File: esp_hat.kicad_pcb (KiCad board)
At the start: 2 copper layers, 65 x 30 mm, 40 parts, among them IC1 AT24CS32-STUM, J1 U.FL, P1 CONN_02X20, P2 CONN_01X03, P3 CONN_01X06, U1 ESP8266EX, U2 AP1117D33, Y1 26MHz

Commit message: Mostly done
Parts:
- added REF**: Symbol_OSHW-Logo_SilkScreen, Symbols:Symbol_OSHW-Logo_SilkScreen, F.Cu at (88.0, 94.3)
- R11: footprint mcuos:0603(1608m)-CHIP-RESISTOR -> mcuos:0603(1608m)
- U2: footprint esp_hat:SOT-223-gndslug -> TO_SOT_Packages_SMD:SOT-223
- W1, W2, W3, W4: footprint Mounting_Holes:MountingHole_3-5mm -> esp_hat:NPTH_Hole_3-5mm
- Y1: footprint mcuos:TXC-7V_xtal -> Crystals:crystal_FA238-TSX3225
- moved C1 0.14 mm to (106.2, 95.6)
- moved C3 0.06 mm to (100.3, 95.6)
- turned Y1 to 180 degrees
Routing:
- net GND: track 282.7 -> 536.7 mm, vias 19 -> 74
- net GPIO5: track 28.7 -> 32.7 mm
- net SD_D1: track 29.4 -> 30.9 mm
- net SD_CMD: track 33.2 -> 34.8 mm
- net SD_D0: track 28.6 -> 30.1 mm
- net SD_D3: track 32.4 -> 33.9 mm
- net SD_CLK: track 27.5 -> 29.0 mm
- net SD_D2: track 30.7 -> 31.8 mm
- net Net-(P2-Pad2): track 28.6 -> 29.3 mm
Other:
- net class 50ohm_oshpark: via_dia 0.6 -> 0.6858
- net class Default: via_dia 0.6 -> 0.6858
- rule trace_min: 0.2 -> 0.1524
- rule via_min_drill: 0.3 -> 0.3302
- rule via_min_size: 0.4 -> 0.6858
- board text added: "ESP HAT"

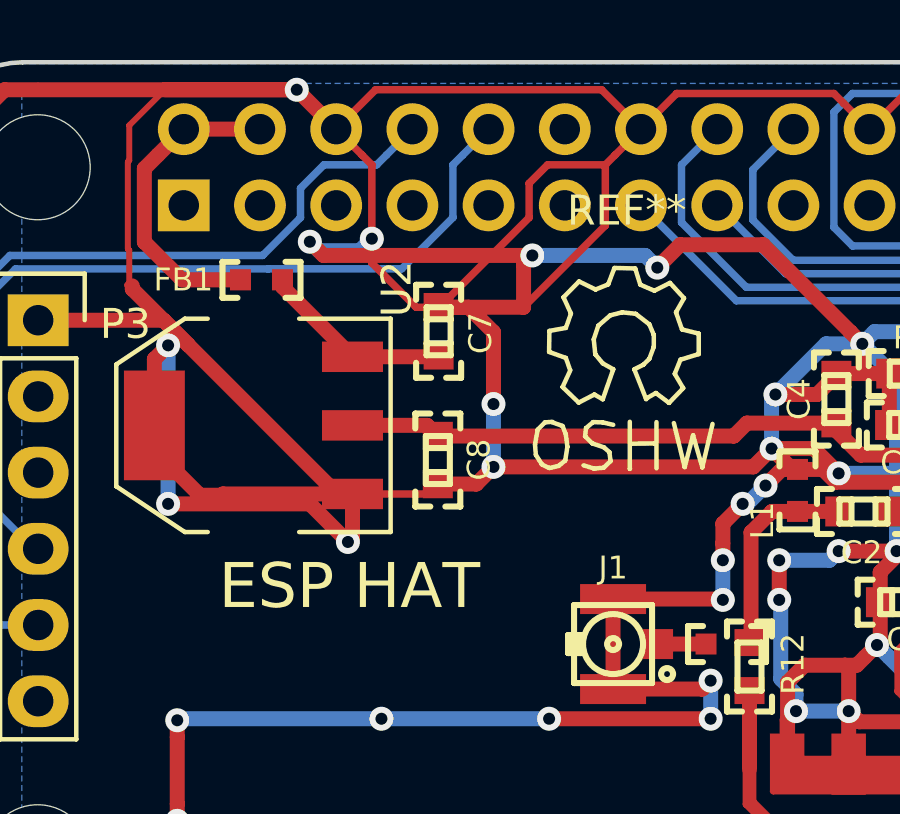
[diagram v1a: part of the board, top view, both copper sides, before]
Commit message: v0.1 to fab, moved text to back silk, changed license to CC-BY-SA
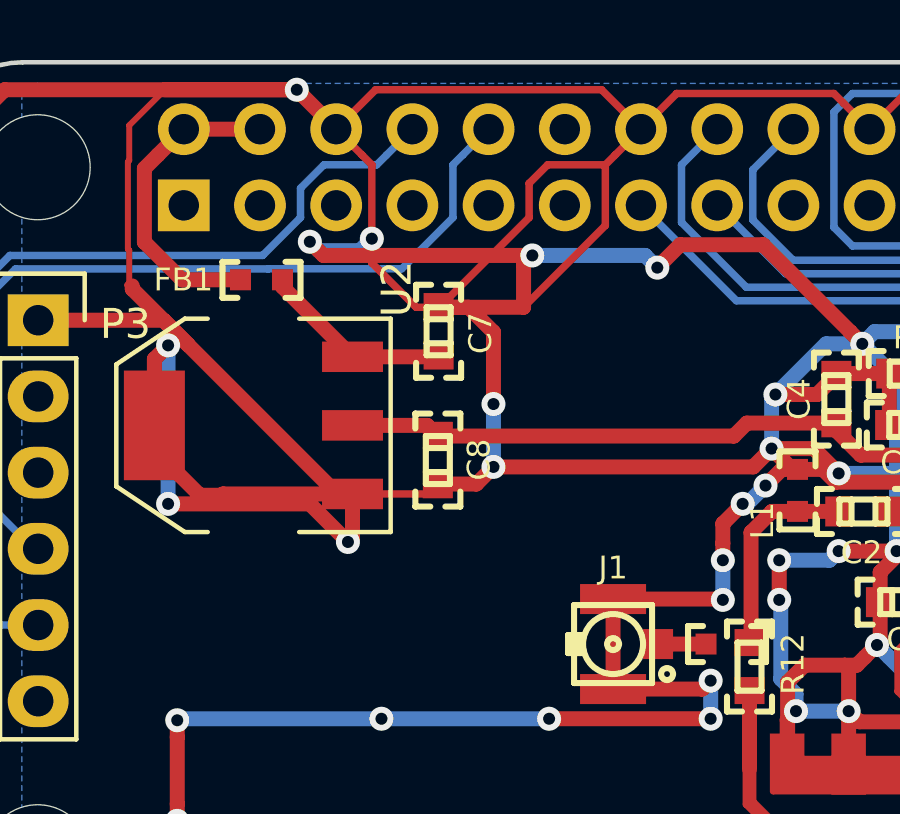
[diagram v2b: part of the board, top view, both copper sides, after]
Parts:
- REF**: moved to B.Cu
- moved REF** 33.2 mm to (119.4, 105.4), turned to 180 degrees
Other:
- board text added: "ESP8xxx WiFi HAT by Andrew Litt 2015-12-11 https://github.com/al177/esp_hat.git"
- board text removed: "ESP HAT"

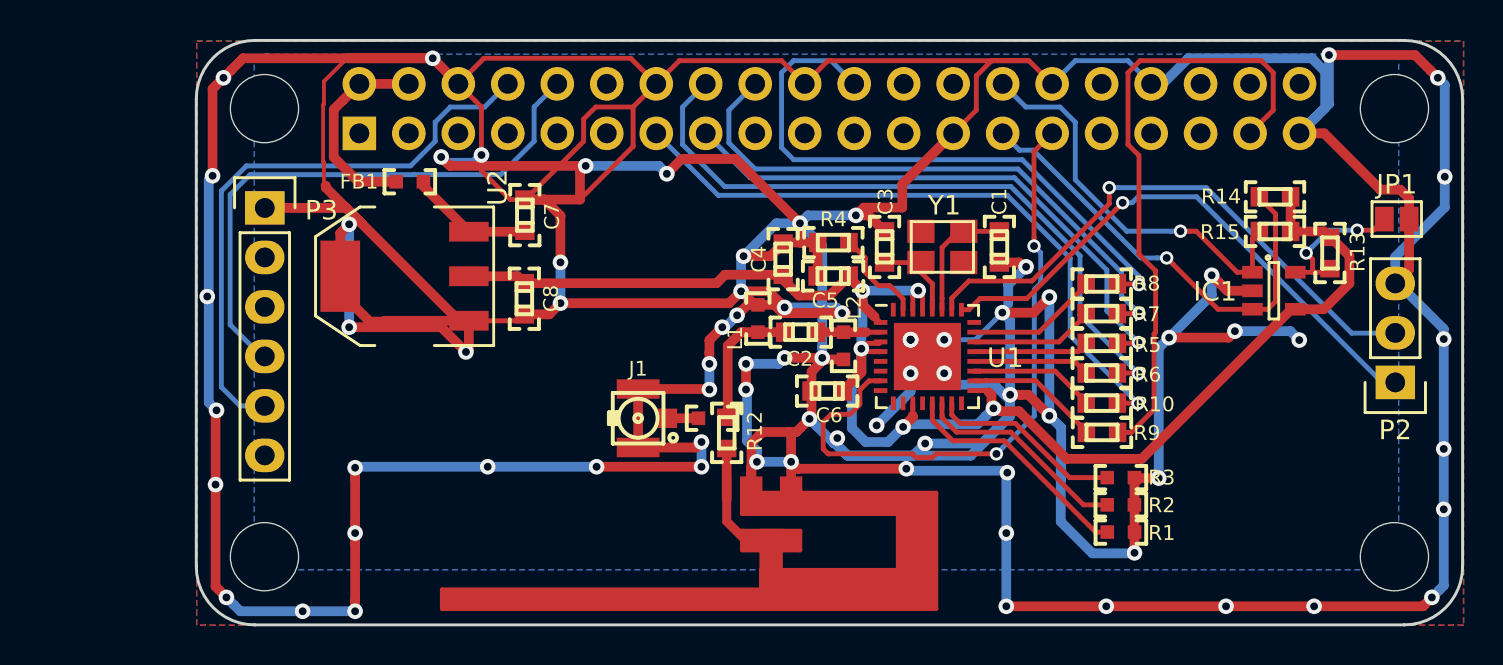
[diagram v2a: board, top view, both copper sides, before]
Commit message: commit v0.2 changes, remove v0.1 fab files
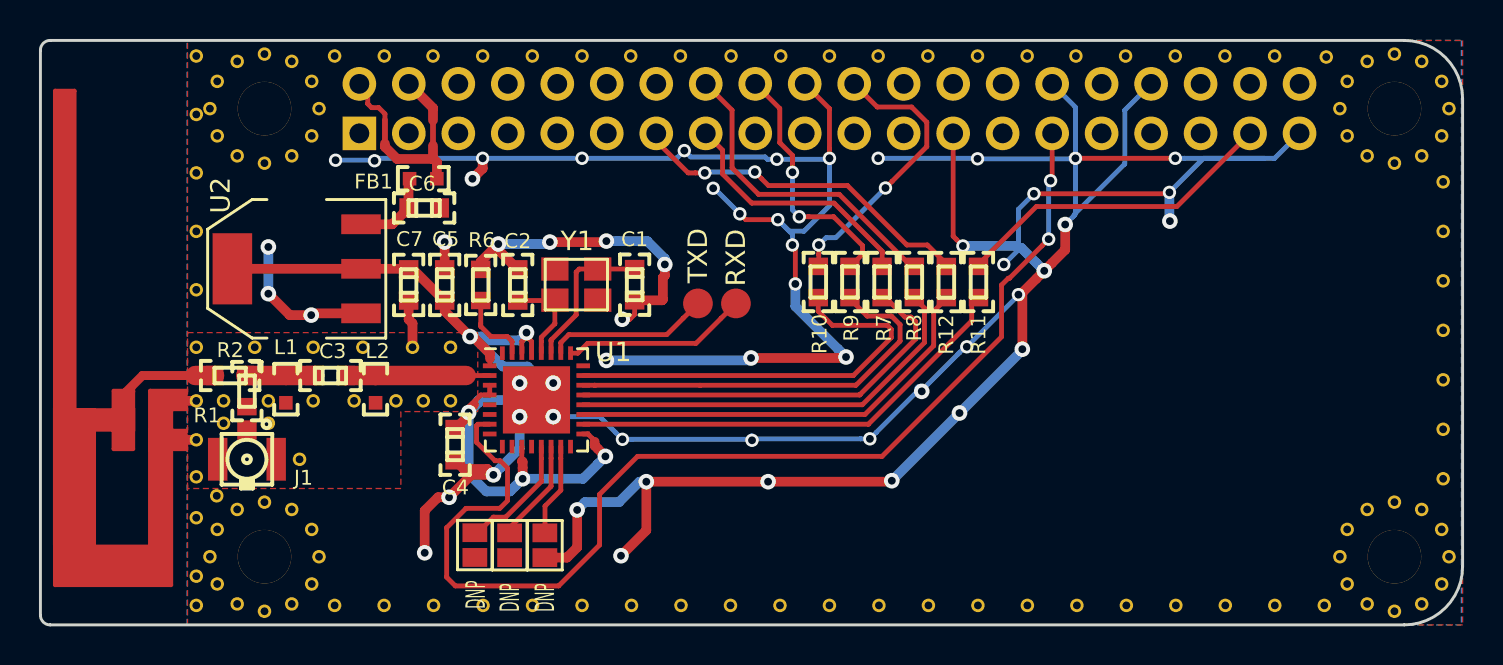
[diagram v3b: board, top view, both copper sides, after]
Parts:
- removed C8: 10uF, mcuos:0603(1608m)-CHIP-CAP
- removed IC1: AT24CS32-STUM, TO_SOT_Packages_SMD:SOT-23-5
- removed JP1: Jumper_NO_Small, Connect:GS2
- removed P2: CONN_01X03, Pin_Headers:Pin_Header_Straight_1x03
- removed P3: CONN_01X06, Pin_Headers:Pin_Header_Straight_1x06
- removed R13: 1K, mcuos:0603(1608m)-CHIP-RESISTOR
- removed R14, R15: 3.9K, mcuos:0603(1608m)-CHIP-RESISTOR
- removed REF**: Symbol_OSHW-Logo_SilkScreen, Symbols:Symbol_OSHW-Logo_SilkScreen
- added REF**1: VIA_0.40mm, esp_hat:VIA_0.40mm, B.Cu at (65.0, 105.5)
- added REF**1: VIA_0.40mm, esp_hat:VIA_0.40mm, F.Cu at (102.5, 85.8)
- added REF**1: VIA_0.40mm, esp_hat:VIA_0.40mm, F.Cu at (100.0, 85.8)
- added REF**1: VIA_0.40mm, esp_hat:VIA_0.40mm, F.Cu at (97.5, 85.8)
- added REF**1: VIA_0.40mm, esp_hat:VIA_0.40mm, F.Cu at (95.0, 85.8)
- added REF**1: VIA_0.40mm, esp_hat:VIA_0.40mm, F.Cu at (92.5, 85.8)
- added REF**1: VIA_0.40mm, esp_hat:VIA_0.40mm, F.Cu at (89.8, 85.8)
- added REF**1: VIA_0.40mm, esp_hat:VIA_0.40mm, F.Cu at (87.3, 85.8)
- added REF**1: VIA_0.40mm, esp_hat:VIA_0.40mm, F.Cu at (84.8, 85.8)
- added REF**1: VIA_0.40mm, esp_hat:VIA_0.40mm, F.Cu at (82.2, 85.8)
- added REF**1: VIA_0.40mm, esp_hat:VIA_0.40mm, F.Cu at (79.7, 85.8)
- added REF**1: VIA_0.40mm, esp_hat:VIA_0.40mm, F.Cu at (123.0, 85.8)
- added REF**1: VIA_0.40mm, esp_hat:VIA_0.40mm, F.Cu at (77.2, 85.8)
- added REF**1: VIA_0.40mm, esp_hat:VIA_0.40mm, F.Cu at (74.7, 85.8)
- added REF**1: VIA_0.40mm, esp_hat:VIA_0.40mm, F.Cu at (72.1, 85.8)
- added REF**1: VIA_0.40mm, esp_hat:VIA_0.40mm, F.Cu at (76.7, 103.5)
- added REF**1: VIA_0.40mm, esp_hat:VIA_0.40mm, F.Cu at (78.0, 100.8)
- added REF**1: VIA_0.40mm, esp_hat:VIA_0.40mm, F.Cu at (78.0, 103.5)
- added REF**1: VIA_0.40mm, esp_hat:VIA_0.40mm, F.Cu at (75.2, 103.5)
- added REF**1: VIA_0.40mm, esp_hat:VIA_0.40mm, F.Cu at (73.1, 103.5)
- added REF**1: VIA_0.40mm, esp_hat:VIA_0.40mm, F.Cu at (71.0, 103.5)
- added REF**1: VIA_0.40mm, esp_hat:VIA_0.40mm, F.Cu at (68.7, 103.5)
- added REF**1: VIA_0.40mm, esp_hat:VIA_0.40mm, F.Cu at (120.3, 85.8)
- added REF**1: VIA_0.40mm, esp_hat:VIA_0.40mm, F.Cu at (66.4, 103.5)
- added REF**1: VIA_0.40mm, esp_hat:VIA_0.40mm, F.Cu at (65.0, 103.5)
- added REF**1: VIA_0.40mm, esp_hat:VIA_0.40mm, F.Cu at (65.0, 100.8)
- added REF**1: VIA_0.40mm, esp_hat:VIA_0.40mm, F.Cu at (65.0, 85.8)
- added REF**1: VIA_0.40mm, esp_hat:VIA_0.40mm, F.Cu at (117.8, 85.8)
- added REF**1: VIA_0.40mm, esp_hat:VIA_0.40mm, F.Cu at (115.2, 85.8)
- added REF**1: VIA_0.40mm, esp_hat:VIA_0.40mm, F.Cu at (112.7, 85.8)
- added REF**1: VIA_0.40mm, esp_hat:VIA_0.40mm, F.Cu at (110.2, 85.8)
- added REF**1: VIA_0.40mm, esp_hat:VIA_0.40mm, F.Cu at (107.7, 85.8)
- added REF**1: VIA_0.40mm, esp_hat:VIA_0.40mm, F.Cu at (105.1, 85.8)
- added REF**101: VIA_0.40mm, esp_hat:VIA_0.40mm, F.Cu at (95.0, 114.0)
- added REF**111: VIA_0.40mm, esp_hat:VIA_0.40mm, F.Cu at (97.5, 114.0)
- added REF**121: VIA_0.40mm, esp_hat:VIA_0.40mm, F.Cu at (100.0, 114.0)
- added REF**131: VIA_0.40mm, esp_hat:VIA_0.40mm, F.Cu at (102.6, 114.0)
- added REF**141: VIA_0.40mm, esp_hat:VIA_0.40mm, F.Cu at (105.1, 114.0)
- added REF**151: VIA_0.40mm, esp_hat:VIA_0.40mm, F.Cu at (107.7, 114.0)
- added REF**161: VIA_0.40mm, esp_hat:VIA_0.40mm, F.Cu at (110.2, 114.0)
- added REF**171: VIA_0.40mm, esp_hat:VIA_0.40mm, F.Cu at (112.7, 114.0)
- added REF**181: VIA_0.40mm, esp_hat:VIA_0.40mm, F.Cu at (115.3, 114.0)
- added REF**191: VIA_0.40mm, esp_hat:VIA_0.40mm, F.Cu at (117.8, 114.0)
- added REF**2: VIA_0.40mm, esp_hat:VIA_0.40mm, F.Cu at (66.0, 108.4)
- added REF**2: VIA_0.40mm, esp_hat:VIA_0.40mm, F.Cu at (66.4, 104.7)
- added REF**2: VIA_0.40mm, esp_hat:VIA_0.40mm, F.Cu at (68.7, 104.7)
- added REF**2: VIA_0.40mm, esp_hat:VIA_0.40mm, F.Cu at (70.3, 106.5)
- added REF**2: VIA_0.40mm, esp_hat:VIA_0.40mm, F.Cu at (65.0, 107.4)
- added REF**2: VIA_0.40mm, esp_hat:VIA_0.40mm, F.Cu at (68.0, 100.8)
- added REF**2: VIA_0.40mm, esp_hat:VIA_0.40mm, F.Cu at (65.0, 88.8)
- added REF**201: VIA_0.40mm, esp_hat:VIA_0.40mm, F.Cu at (120.4, 114.0)
- added REF**211: VIA_0.40mm, esp_hat:VIA_0.40mm, F.Cu at (122.9, 114.0)
- added REF**211: VIA_0.40mm, esp_hat:VIA_0.40mm, F.Cu at (74.6, 114.0)
- added REF**21111: VIA_0.40mm, esp_hat:VIA_0.40mm, F.Cu at (129.0, 107.5)
- added REF**21112: VIA_0.40mm, esp_hat:VIA_0.40mm, F.Cu at (129.0, 105.0)
- added REF**21113: VIA_0.40mm, esp_hat:VIA_0.40mm, F.Cu at (129.0, 102.4)
- added REF**21114: VIA_0.40mm, esp_hat:VIA_0.40mm, F.Cu at (129.0, 99.9)
- added REF**21115: VIA_0.40mm, esp_hat:VIA_0.40mm, F.Cu at (129.0, 97.3)
- added REF**21116: VIA_0.40mm, esp_hat:VIA_0.40mm, F.Cu at (129.0, 94.8)
- added REF**21117: VIA_0.40mm, esp_hat:VIA_0.40mm, F.Cu at (129.0, 92.3)
- added REF**221: VIA_0.40mm, esp_hat:VIA_0.40mm, F.Cu at (72.1, 114.0)
- added REF**3: VIA_0.40mm, esp_hat:VIA_0.40mm, F.Cu at (65.0, 109.5)
- added REF**3: VIA_0.40mm, esp_hat:VIA_0.40mm, F.Cu at (71.0, 100.8)
- added REF**3: VIA_0.40mm, esp_hat:VIA_0.40mm, F.Cu at (65.0, 91.8)
- added REF**31: VIA_0.40mm, esp_hat:VIA_0.40mm, F.Cu at (77.2, 114.0)
- added REF**4: VIA_0.40mm, esp_hat:VIA_0.40mm, F.Cu at (65.0, 114.0)
- added REF**4: VIA_0.40mm, esp_hat:VIA_0.40mm, F.Cu at (65.0, 112.5)
- added REF**4: VIA_0.40mm, esp_hat:VIA_0.40mm, F.Cu at (73.5, 100.8)
- added REF**4: VIA_0.40mm, esp_hat:VIA_0.40mm, F.Cu at (65.0, 94.8)
- added REF**41: VIA_0.40mm, esp_hat:VIA_0.40mm, F.Cu at (79.7, 114.0)
- added REF**5: VIA_0.40mm, esp_hat:VIA_0.40mm, F.Cu at (76.1, 100.8)
- added REF**5: VIA_0.40mm, esp_hat:VIA_0.40mm, F.Cu at (65.0, 97.8)
- added REF**51: VIA_0.40mm, esp_hat:VIA_0.40mm, F.Cu at (82.3, 114.0)
- added REF**61: VIA_0.40mm, esp_hat:VIA_0.40mm, F.Cu at (84.8, 114.0)
- added REF**71: VIA_0.40mm, esp_hat:VIA_0.40mm, F.Cu at (87.3, 114.0)
- added REF**81: VIA_0.40mm, esp_hat:VIA_0.40mm, F.Cu at (89.9, 114.0)
- added REF**91: VIA_0.40mm, esp_hat:VIA_0.40mm, F.Cu at (92.4, 114.0)
- added W5: MOUNT, esp_hat:NPTH_Hole_2_75mm, F.Cu at (126.5, 111.5)
- added W6: MOUNT, esp_hat:NPTH_Hole_2_75mm, F.Cu at (126.5, 88.5)
- ANT1: footprint SH_Antennas:TI_DN007_2.4GHz -> esp_hat:TI_DN007_2.4GHz
- C2: value 5.6pF -> 10pF
- C3: value 10pF -> 5.6pF
- C4: value 10uF -> 0.1uF
- C5: value 1uF -> 0.1uF
- C6: value 0.1uF -> 10uF
- R1: footprint mcuos:0603(1608m) -> mcuos:0603(1608m)-CHIP-RESISTOR
- R11: value DNP -> 200; footprint mcuos:0603(1608m) -> mcuos:0603(1608m)-CHIP-RESISTOR
- R12: value 0 -> 200
- R2: value DNP -> 0; footprint mcuos:0603(1608m) -> mcuos:0603(1608m)-CHIP-RESISTOR
- R3: footprint mcuos:0603(1608m) -> Connect:GS2
- R4: value 12.0K -> DNP; footprint mcuos:0603(1608m)-CHIP-RESISTOR -> Connect:GS2
- R5: value 200 -> DNP; footprint mcuos:0603(1608m)-CHIP-RESISTOR -> Connect:GS2
- R6: value 200 -> 12.0K
- U2: footprint TO_SOT_Packages_SMD:SOT-223 -> esp_hat:SOT-223-REG_VOUTSLUG
- W1: value TEST_1P -> RXD; footprint esp_hat:NPTH_Hole_3-5mm -> Measurement_Points:Measurement_Point_Round-SMD-Pad_Small
- W2: value TEST_1P -> TXD; footprint esp_hat:NPTH_Hole_3-5mm -> Measurement_Points:Measurement_Point_Round-SMD-Pad_Small
- W3, W4: value TEST_1P -> MOUNT; footprint esp_hat:NPTH_Hole_3-5mm -> esp_hat:NPTH_Hole_2_75mm
- moved W3 62.4 mm to (68.5, 88.5)
- moved W4 62.4 mm to (68.5, 111.5)
- moved R2 46.2 mm to (66.7, 102.2)
- moved R1 45.4 mm to (67.6, 103.0), turned to 270 degrees
- moved R3 33.3 mm to (79.3, 110.9)
- moved R6 32.2 mm to (79.6, 97.5), turned to 270 degrees
- moved ANT1 31.4 mm to (60.8, 100.3), turned to 90 degrees
- moved R5 30.4 mm to (82.9, 110.9), turned to 0 degrees
- moved C3 29.2 mm to (71.9, 102.2), turned to 180 degrees
- moved W1 27.5 mm to (92.7, 98.5)
- moved L1 24.5 mm to (69.6, 102.9), turned to 270 degrees
- moved W2 24.4 mm to (90.8, 98.5)
- moved L2 24.1 mm to (74.2, 102.9)
- moved R4 22.7 mm to (81.1, 110.9)
- moved C6 22.7 mm to (76.7, 93.6), turned to 0 degrees
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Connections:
- C2 pad 1: /50ohm_LNA -> Net-(C2-Pad1)
- C2 pad 2: /50ohm_filt -> GND
- C3 pad 1: Net-(C3-Pad1) -> /50ohm_LNA
- C3 pad 2: GND -> /50ohm_filt
- C6 pad 1: +3V3 -> /5V_filt
- C7 pad 1: /5V_filt -> +3V3
- P1 pad 10: PI_UART0_RXD -> (no net)
- P1 pad 27: ID_SD -> (no net)
- P1 pad 28: ID_SC -> (no net)
- P1 pad 8: PI_UART0_TXD -> (no net)
- R1 pad 1: Net-(R1-Pad1) -> /50ohm_filt
- R1 pad 2: GND -> /50ohm_ufl
- R10 pad 1: SD_D3 -> SD_D1
- R11 pad 1: /50ohm_filt -> SD_D2
- R11 pad 2: /50ohm_ufl -> Net-(R11-Pad2)
- R12 pad 1: /50ohm_ant -> SD_D3
- R12 pad 2: /50ohm_filt -> Net-(R12-Pad2)
- R2 pad 1: Net-(R2-Pad1) -> /50ohm_ant
- R2 pad 2: GND -> /50ohm_filt
- R4 pad 1: GND -> Net-(R4-Pad1)
- R4 pad 2: Net-(R4-Pad2) -> GND
- R5 pad 1: SD_CLK -> Net-(R5-Pad1)
- R5 pad 2: Net-(R5-Pad2) -> GND
- R6 pad 1: SD_CMD -> GND
- R7 pad 1: SD_D0 -> SD_CLK
- R8 pad 1: SD_D1 -> SD_CMD
- R9 pad 1: SD_D2 -> SD_D0
- U1 pad 13: Net-(R1-Pad1) -> Net-(R3-Pad1)
- U1 pad 14: Net-(R2-Pad1) -> Net-(R4-Pad1)
- U1 pad 15: Net-(R3-Pad1) -> Net-(R5-Pad1)
- U1 pad 18: Net-(R9-Pad2) -> Net-(R11-Pad2)
- U1 pad 19: Net-(R10-Pad2) -> Net-(R12-Pad2)
- U1 pad 20: Net-(R6-Pad2) -> Net-(R8-Pad2)
- U1 pad 21: Net-(R5-Pad2) -> Net-(R7-Pad2)
- U1 pad 22: Net-(R7-Pad2) -> Net-(R9-Pad2)
- U1 pad 23: Net-(R8-Pad2) -> Net-(R10-Pad2)
- U1 pad 25: Net-(P2-Pad1) -> Net-(U1-Pad25)
- U1 pad 26: Net-(P2-Pad2) -> Net-(U1-Pad26)
- U1 pad 28: Net-(C3-Pad1) -> Net-(C2-Pad1)
- U1 pad 31: Net-(R4-Pad2) -> Net-(R6-Pad2)
- Y1 pad 2: Net-(C3-Pad1) -> Net-(C2-Pad1)
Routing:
- net GND: track 536.7 -> 250.6 mm, vias 74 -> 56
- net +3V3: track 82.5 -> 48.0 mm
- net PI_UART0_TXD: track 30.2 -> 0.00 mm
- net PI_UART0_RXD: track 29.3 -> 0.00 mm
- net Net-(P2-Pad2): track 29.3 -> 0.00 mm, vias 1 -> 0
- net Net-(P2-Pad1): track 28.6 -> 0.00 mm, vias 1 -> 0
- net GPIO5: track 32.7 -> 58.7 mm
- net Net-(R11-Pad2): track 0.00 -> 23.7 mm
- net ID_SD: track 23.6 -> 0.00 mm, vias 1 -> 0
- net Net-(R12-Pad2): track 0.00 -> 22.2 mm
- net ID_SC: track 20.8 -> 0.00 mm, vias 1 -> 0
- net SD_CMD: track 34.8 -> 16.3 mm, vias 1 -> 0
- net SD_D0: track 30.1 -> 13.0 mm, vias 1 -> 2
- net SD_D1: track 30.9 -> 14.6 mm, vias 1 -> 2
- net SD_CLK: track 29.0 -> 13.1 mm, vias 1 -> 0
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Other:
- board size 65 x 30 mm -> 73 x 30 mm
- net class 50ohm_oshpark: clearance 0.05 -> 0.15; trace_width 0.5 -> 1
- board text added: "max skew must be <250mil variance as routed is 235mil"
- board text removed: "ESP8xxx WiFi HAT by Andrew Litt 2015-12-11 https://github.com/al177/esp_hat.git"
